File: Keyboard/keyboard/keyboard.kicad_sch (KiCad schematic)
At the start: 0 parts

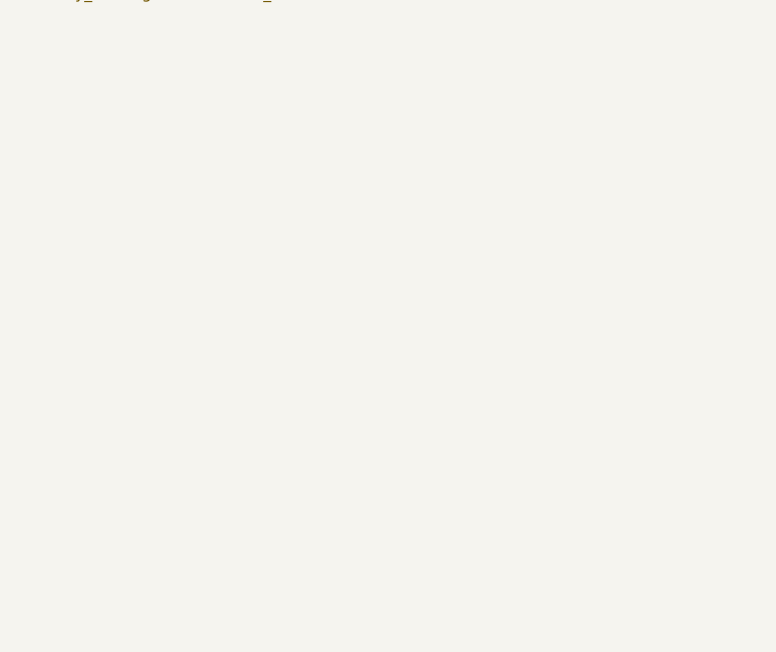
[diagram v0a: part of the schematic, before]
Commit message: fixing keyboard and pot project schematics
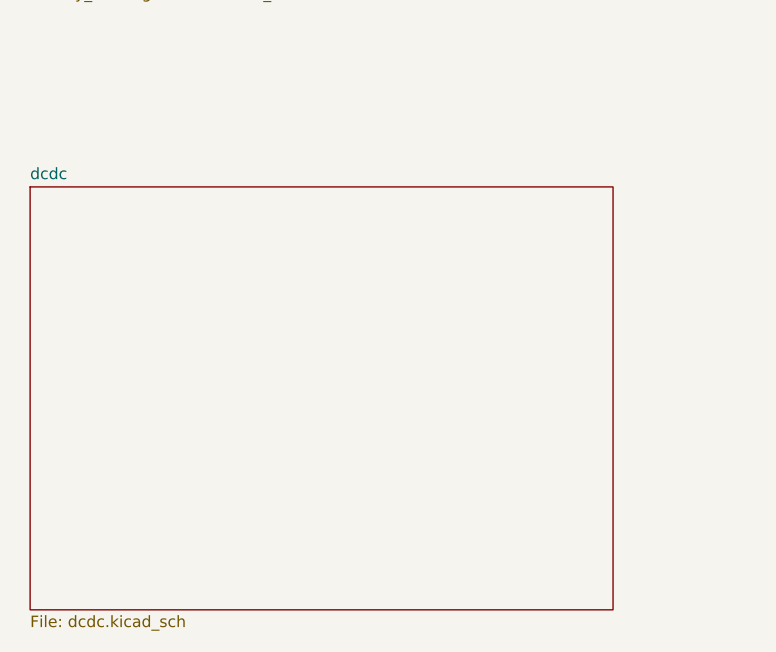
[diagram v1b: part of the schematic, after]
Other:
- added sheet dcdc (dcdc.kicad_sch)
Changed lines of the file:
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@@
 (kicad_sch (version 20211123) (generator eeschema)
   (paper "A4")
+  (sheet (at 41.91 127) (size 64.77 46.99) (fields_autoplaced)
+    (stroke (width 0.1524) (type solid) (color 0 0 0 0))
+    (fill (color 0 0 0 0.0000))
+    (property "Sheet name" "dcdc" (id 0) (at 41.91 126.2884 0)
+      (effects (font (size 1.27 1.27)) (justify left bottom))
+    )
+    (property "Sheet file" "dcdc.kicad_sch" (id 1) (at 41.91 174.5746 0)
+      (effects (font (size 1.27 1.27)) (justify left top))
+    )
+  )
   (sheet (at 147.32 29.21) (size 63.5 74.93) (fields_autoplaced)
     (stroke (width 0.1524) (type solid) (color 0 0 0 0))
@@
     (path "/f28e56e7-283b-4b9a-ae27-95e89770fbf8" (page "2"))
     (path "/31ae1ddb-55f8-4875-b94d-87a4d0c86414" (page "3"))
+    (path "/1102bd9a-5afc-41a6-b521-47e47bf6e05c" (page "4"))
   )
   (symbol_instances
-    (path "/f28e56e7-283b-4b9a-ae27-95e89770fbf8/a89d54cc-daae-4e15-9b3e-03af93558223"
-      (reference "#PWR01") (unit 1) (value "GND") (footprint "")
+    (path "/f28e56e7-283b-4b9a-ae27-95e89770fbf8/0747aa35-9275-422f-9427-eb99ab7055a3"
+      (reference "#PWR01") (unit 1) (value "+3.3V") (footprint "")
     )
     (path "/f28e56e7-283b-4b9a-ae27-95e89770fbf8/c10bdb93-40f2-4534-a38d-7f700adc998a"
@@
       (reference "#PWR05") (unit 1) (value "GND") (footprint "")
     )
-    (path "/f28e56e7-283b-4b9a-ae27-95e89770fbf8/d3c5db6a-db5d-4dea-bf4d-765dc4456b55"
+    (path "/f28e56e7-283b-4b9a-ae27-95e89770fbf8/03899fc2-7ab8-4d54-82c2-1488f5d9b0d9"
       (reference "#PWR06") (unit 1) (value "+3.3V") (footprint "")
     )
@@
       (reference "#PWR010") (unit 1) (value "+3.3V") (footprint "")
     )
+    (path "/f28e56e7-283b-4b9a-ae27-95e89770fbf8/a2689e5c-8ccd-4e2c-8098-087f3c734022"
+      (reference "#PWR011") (unit 1) (value "+3.3V") (footprint "")
+    )
+    (path "/f28e56e7-283b-4b9a-ae27-95e89770fbf8/48b4ad4e-8205-4f00-b73b-d8c0cd629233"
+      (reference "#PWR012") (unit 1) (value "GND") (footprint "")
+    )
+    (path "/f28e56e7-283b-4b9a-ae27-95e89770fbf8/2ac31afe-6dde-403d-bbdc-3366c8b144f8"
+      (reference "#PWR013") (unit 1) (value "GND") (footprint "")
+    )
+    (path "/1102bd9a-5afc-41a6-b521-47e47bf6e05c/b25fa862-95a1-42c3-bfae-6757344695e5"
+      (reference "#PWR014") (unit 1) (value "GND") (footprint "")
+    )
+    (path "/1102bd9a-5afc-41a6-b521-47e47bf6e05c/3f31be44-1d8e-483b-8a17-68ceff23fd83"
+      (reference "#PWR015") (unit 1) (value "+3.3V") (footprint "")
+    )
     (path "/f28e56e7-283b-4b9a-ae27-95e89770fbf8/6182ca9b-1bd4-4f37-bff8-2540085c3fe2"
       (reference "C1") (unit 1) (value "100nF") (footprint "Capacitor_SMD:C_0805_2012Metric_Pad1.18x1.45mm_HandSolder")
@@
       (reference "C2") (unit 1) (value "100nF") (footprint "Capacitor_SMD:C_0805_2012Metric_Pad1.18x1.45mm_HandSolder")
     )
-    (path "/f28e56e7-283b-4b9a-ae27-95e89770fbf8/d6438a44-b742-48ae-b52f-11da0511314b"
-      (reference "C3") (unit 1) (value "4.7u") (footprint "Capacitor_SMD:C_0805_2012Metric_Pad1.18x1.45mm_HandSolder")
+    (path "/f28e56e7-283b-4b9a-ae27-95e89770fbf8/f4a3a393-4fce-4cf2-827d-21790fb5141b"
+      (reference "C3") (unit 1) (value "100nF") (footprint "Capacitor_SMD:C_0805_2012Metric_Pad1.18x1.45mm_HandSolder")
+    )
+    (path "/1102bd9a-5afc-41a6-b521-47e47bf6e05c/9eb21eb1-e612-454b-9cb2-6ca26ae057e8"
+      (reference "C4") (unit 1) (value "22uF") (footprint "Capacitor_SMD:C_0805_2012Metric_Pad1.18x1.45mm_HandSolder")
+    )
+    (path "/1102bd9a-5afc-41a6-b521-47e47bf6e05c/c6ddc4db-fc52-4704-b8ee-9f99e25bd000"
+      (reference "C5") (unit 1) (value "2.2uF") (footprint "Capacitor_SMD:C_0805_2012Metric_Pad1.18x1.45mm_HandSolder")
+    )
+    (path "/1102bd9a-5afc-41a6-b521-47e47bf6e05c/98bfd018-32df-478e-a5a4-552ef5539af2"
+      (reference "C6") (unit 1) (value "2.2nF") (footprint "Capacitor_SMD:C_0805_2012Metric_Pad1.18x1.45mm_HandSolder")
+    )
+    (path "/1102bd9a-5afc-41a6-b521-47e47bf6e05c/014be2d6-ffe7-4a51-abde-fe976d3833f8"
+      (reference "C7") (unit 1) (value "10uF") (footprint "Capacitor_SMD:C_0805_2012Metric_Pad1.18x1.45mm_HandSolder")
+    )
+    (path "/1102bd9a-5afc-41a6-b521-47e47bf6e05c/af6bfc13-7434-49c5-b0b6-004baf74fd8c"
+      (reference "C8") (unit 1) (value "?uF") (footprint "Capacitor_SMD:C_0805_2012Metric_Pad1.18x1.45mm_HandSolder")
     )
     (path "/31ae1ddb-55f8-4875-b94d-87a4d0c86414/4922a27f-2fc0-4024-8b8c-fc608e3df5fe"
@@
       (reference "D12") (unit 1) (value "LL4148") (footprint "Diode_SMD:D_MiniMELF")
     )
-    (path "/f28e56e7-283b-4b9a-ae27-95e89770fbf8/a57c8f49-d8f4-4111-9a42-6f40731d2058"
-      (reference "J1") (unit 1) (value "Conn_01x06_Male") (footprint "Connector_PinSocket_2.54mm:PinSocket_1x06_P2.54mm_Horizontal")
+    (path "/1102bd9a-5afc-41a6-b521-47e47bf6e05c/43a1ce24-08e9-4e4e-806b-5c52aacae56d"
+      (reference "D13") (unit 1) (value "FUXINSEMI DSK34 (SOD-123)") (footprint "Diode_SMD:D_SOD-123")
+    )
+    (path "/f28e56e7-283b-4b9a-ae27-95e89770fbf8/b69731dc-a74d-4be9-8b11-0a21dad4be18"
+      (reference "J1") (unit 1) (value "Conn_01x05_Male") (footprint "")
     )
     (path "/f28e56e7-283b-4b9a-ae27-95e89770fbf8/6cbc6b9c-37f8-4d4a-9780-7abd8c87c83f"
       (reference "J2") (unit 1) (value "Conn_01x06_Male") (footprint "")
     )
+    (path "/1102bd9a-5afc-41a6-b521-47e47bf6e05c/33f3bdd1-b296-45cf-aa20-3cbbf6ec1e9c"
+      (reference "L1") (unit 1) (value "6.8uH") (footprint "inductors:inductor_koherelec")
+    )
+    (path "/1102bd9a-5afc-41a6-b521-47e47bf6e05c/a431f423-00c7-4287-b2d8-c93a3b03663b"
+      (reference "L2") (unit 1) (value "6.8uH") (footprint "inductors:inductor_koherelec")
+    )
     (path "/f28e56e7-283b-4b9a-ae27-95e89770fbf8/5f70a067-b3bd-48a3-8ea3-c9f50586f7c5"
       (reference "R1") (unit 1) (value "10k") (footprint "Resistor_SMD:R_0805_2012Metric_Pad1.20x1.40mm_HandSolder")
@@
       (reference "R4") (unit 1) (value "10K") (footprint "Resistor_SMD:R_0805_2012Metric_Pad1.20x1.40mm_HandSolder")
     )
+    (path "/f28e56e7-283b-4b9a-ae27-95e89770fbf8/71d384ef-6541-4d3f-8e57-b50845e9c714"
+      (reference "R5") (unit 1) (value "100k") (footprint "Resistor_SMD:R_0805_2012Metric_Pad1.20x1.40mm_HandSolder")
+    )
+    (path "/1102bd9a-5afc-41a6-b521-47e47bf6e05c/006588d8-bd80-4a9e-8dad-cff9494e67a1"
+      (reference "R6") (unit 1) (value "100K") (footprint "Resistor_SMD:R_0805_2012Metric_Pad1.20x1.40mm_HandSolder")
+    )
+    (path "/1102bd9a-5afc-41a6-b521-47e47bf6e05c/b0786aa3-3180-48a4-9fce-5a35c8c82408"
+      (reference "R7") (unit 1) (value "9.1k") (footprint "Resistor_SMD:R_0805_2012Metric_Pad1.20x1.40mm_HandSolder")
+    )
+    (path "/1102bd9a-5afc-41a6-b521-47e47bf6e05c/f2488828-6617-42d5-8a1e-063056c192e4"
+      (reference "R8") (unit 1) (value "5.6k") (footprint "Resistor_SMD:R_0805_2012Metric_Pad1.20x1.40mm_HandSolder")
+    )
     (path "/f28e56e7-283b-4b9a-ae27-95e89770fbf8/dd47cbe3-ce37-4721-a15f-85bb741a8695"
       (reference "SW1") (unit 1) (value "SW_Push") (footprint "")
@@
       (reference "U1") (unit 1) (value "STM32G030K6T6") (footprint "footprints:LQFP-32")
     )
-  )
+    (path "/1102bd9a-5afc-41a6-b521-47e47bf6e05c/a1607e32-a940-440e-869c-63d66eca7e1a"
+      (reference "U2") (unit 1) (value "LMR62421XMF") (footprint "Package_TO_SOT_SMD:SOT-23-5")
+    )
+  )
